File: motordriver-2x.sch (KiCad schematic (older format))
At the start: 330 parts

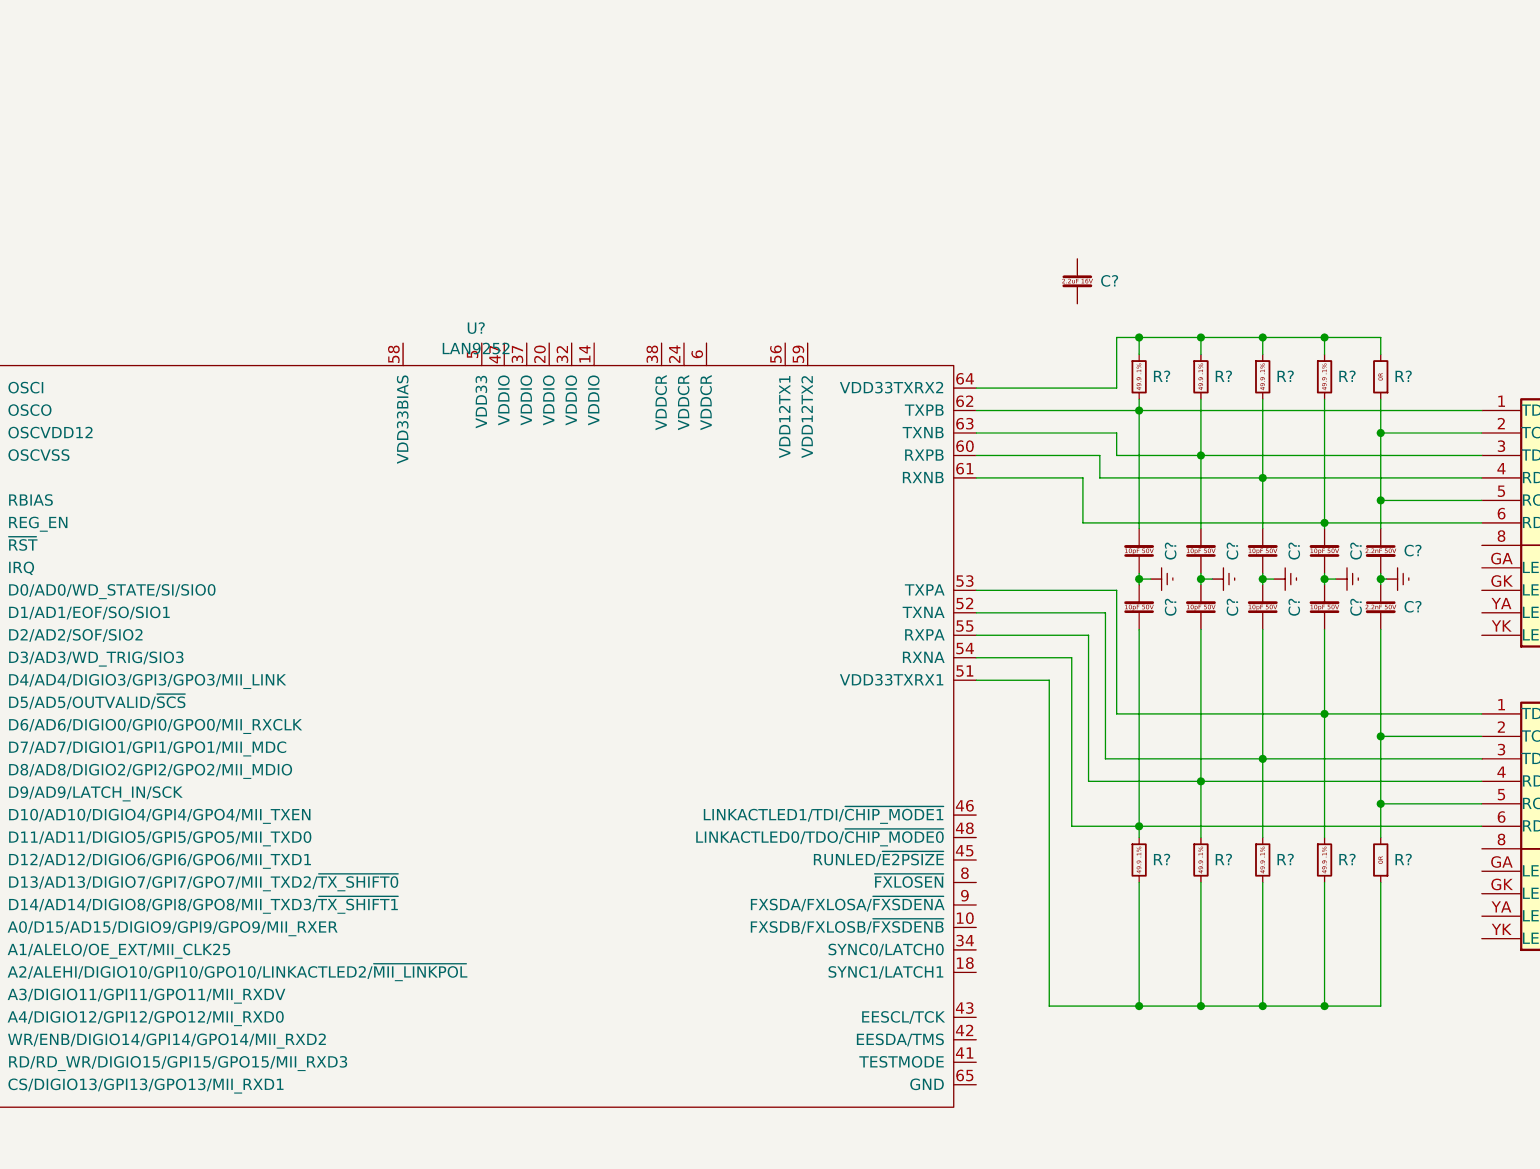
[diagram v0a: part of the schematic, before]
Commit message: add lcd connector
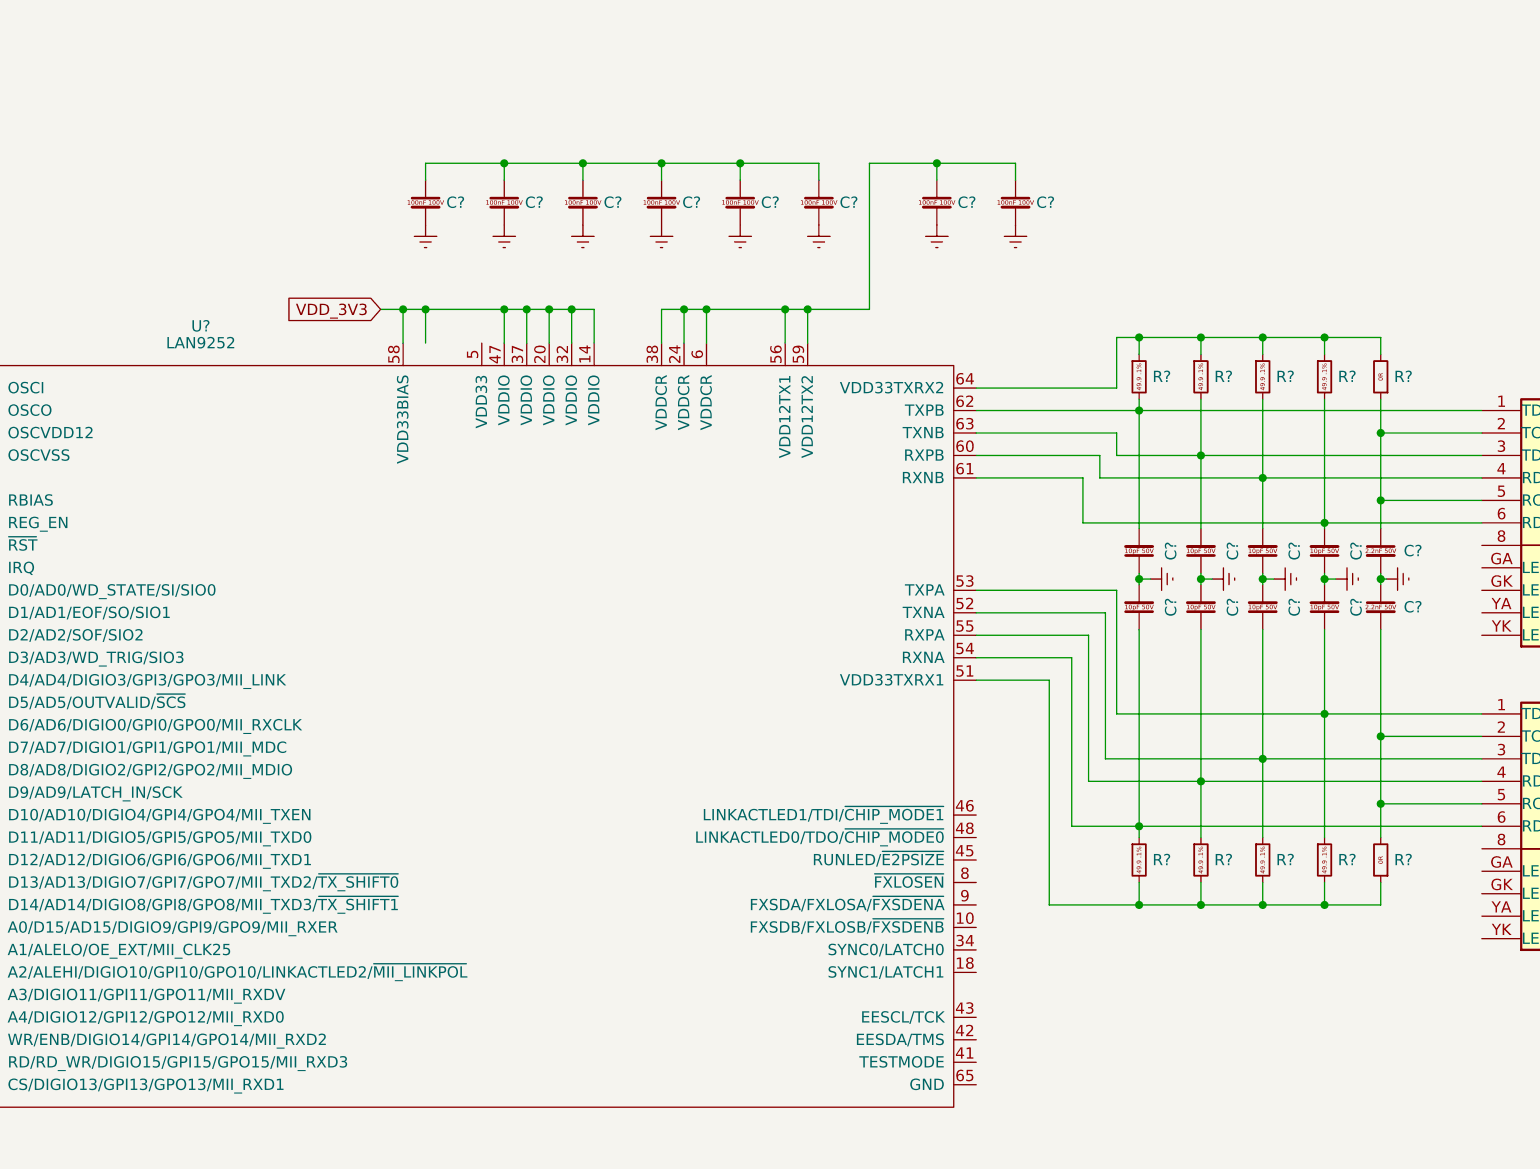
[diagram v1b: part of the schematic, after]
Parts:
- removed C?: CAP_2.2uF_16V_0402, Capacitor_SMD:C_0402_1005Metric, symbol SwEmb:CAP_2.2uF_16V_0402
- added C? (x8): CAP_100nF_100V_0603, Capacitor_SMD:C_0603_1608Metric, symbol SwEmb:CAP_100nF_100V_0603
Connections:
- wire segments 1049 -> 1089

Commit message: work on the ethercat circuit
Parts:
- added C? (x3): CAP_100nF_100V_0603, Capacitor_SMD:C_0603_1608Metric, symbol SwEmb:CAP_100nF_100V_0603
- added C? (x2): CAP_10pF_50V_0402, Capacitor_SMD:C_0402_1005Metric, symbol SwEmb:CAP_10pF_50V_0402
- added C?: CAP_100nF_50V_0402, Capacitor_SMD:C_0402_1005Metric, symbol SwEmb:CAP_100nF_50V_0402
- added D?: D_BAT54S, Package_TO_SOT_SMD:SOT-23, symbol SwEmb:D_BAT54S
- added FB? (x4): LB_220R_2A_0603, Inductor_SMD:L_0603_1608Metric, symbol SwEmb:LB_220R_2A_0603
- added R?: RES_12.1K_1%_0402, Resistor_SMD:R_0402_1005Metric, symbol SwEmb:RES_12.1K_1%_0402
- added R? (x7): RES_10K_1%_0402, Resistor_SMD:R_0402_1005Metric, symbol SwEmb:RES_10K_1%_0402
- added R? (x2): RES_3K_1%_0402, Resistor_SMD:R_0402_1005Metric, symbol SwEmb:RES_3K_1%_0402
- added R? (x2): RES_270R_1%_0402, Resistor_SMD:R_0402_1005Metric, symbol SwEmb:RES_270R_1%_0402
- added U?: IC_M24C02, Package_SO:SOIC-8_3.9x4.9mm_P1.27mm, symbol SwEmb:IC_M24C16
- added Y?: XTAL_25MHz_3225, Crystal:Crystal_SMD_3225-4Pin_3.2x2.5mm, symbol SwEmb:XTAL_25MHz_3225
- U?: symbol SwEmb:IC_M24C02 -> SwEmb:IC_M24C16
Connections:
- net labels added: ECAT_CS, ECAT_IRQ, ECAT_MISO, ECAT_MOSI, ECAT_RESET, ECAT_SCK, ECAT_SYNC0, ECAT_SYNC1
- wire segments 1089 -> 1191
- no-connect marks 30 -> 38
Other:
- note added: "150mA"

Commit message: add main power
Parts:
- added C?: CAPP_220uF_63V_10x15_THT, Capacitor_THT:CP_Radial_D10.0mm_P5.00mm, symbol SwEmb:CAPP_220uF_63V_10x15_THT
- added C?: CAP_27nF_16V_0402, Capacitor_SMD:C_0402_1005Metric, symbol SwEmb:CAP_27nF_16V_0402
- added C?: CAP_100nF_50V_0402, Capacitor_SMD:C_0402_1005Metric, symbol SwEmb:CAP_100nF_50V_0402
- added C?: CAP_51pF_50V_0402, Capacitor_SMD:C_0402_1005Metric, symbol SwEmb:CAP_51pF_50V_0402
- added C?: CAPP_100uF_25V_6357, Capacitor_SMD:CP_Elec_6.3x5.7, symbol SwEmb:CAPP_100uF_25V_6357
- added D?: D_CDBC5100, Diode_SMD:D_SMC, symbol SwEmb:D_CDBC5100
- added L?: L_100uH_3.64A, CUSTOM:L_Wuerth_WE-PD-Typ-LS_1250x1250, symbol SwEmb:L_100uH_3.64A
- added R?: RES_1M_1%_0402, Resistor_SMD:R_0402_1005Metric, symbol SwEmb:RES_1M_1%_0402
- added R?: RES_5K_1%_0402, Resistor_SMD:R_0402_1005Metric, symbol SwEmb:RES_5K_1%_0402
- added R?: RES_10K_1%_0402, Resistor_SMD:R_0402_1005Metric, symbol SwEmb:RES_10K_1%_0402
- added R?: RES_147k_1%_0603, Resistor_SMD:R_0603_1608Metric, symbol SwEmb:RES_147k_1%_0603
- added R?: RES_10.5k_1%_0603, Resistor_SMD:R_0603_1608Metric, symbol SwEmb:RES_10.5k_1%_0603
- added U?: IC_TPS54360DDA, SOIC:SOIC127P600X175_HS-9N, symbol SwEmb:IC_TPS54360DDA
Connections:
- net GNDREF: now also D?.1, D?.1, D?.1, D?.1, D?.1, D?.1, D?.1, C?.2, C?.2, C?.2, C?.2, D?.2 (A), R?.2, R?.2, U?.7 (GND), U?.9 (GNDPAD)
- net VDD_3V3: now also D?.2, D?.2, D?.2, D?.2, D?.2, D?.2, D?.2
- net VMOT_SENSE: now also D?.3
- net VSA1: now also D?.3
- net VSA2: now also D?.3
- net VSB1: now also D?.3
- net VSB2: now also D?.3
- net VSC1: now also D?.3
- net VSC2: now also D?.3
- new net: C?.2, U?.1 (BOOT)
- new net: C?.1, U?.2 (VIN)
- new net: R?.1, U?.4 (RT/CLK)
- new net: R?.1, R?.2, U?.5 (FB)
- new net: C?.1, R?.1, U?.6 (COMP)
- new net: C?.1, D?.1 (K), L?.1, U?.8 (SW)
- new net: C?.1, R?.2
- new net: R?.1, R?.2
- new net: C?.1, L?.2, R?.1
- no-connect marks 38 -> 39

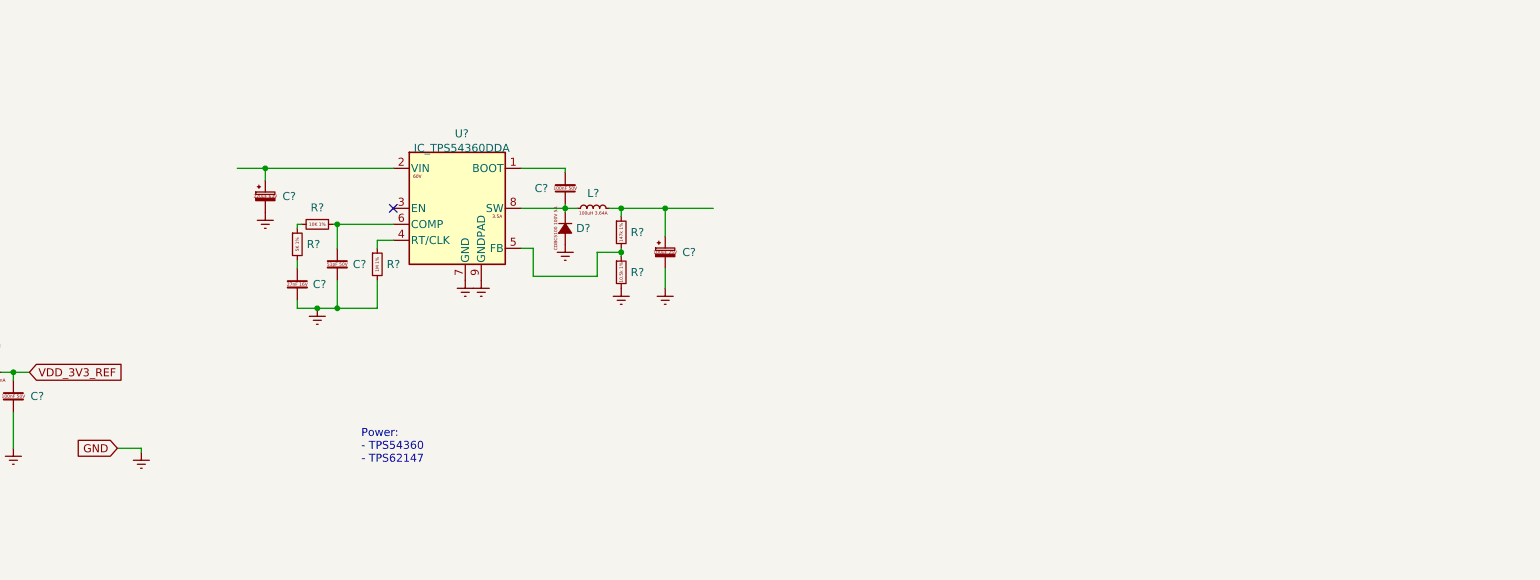
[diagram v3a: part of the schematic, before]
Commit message: add power supplies
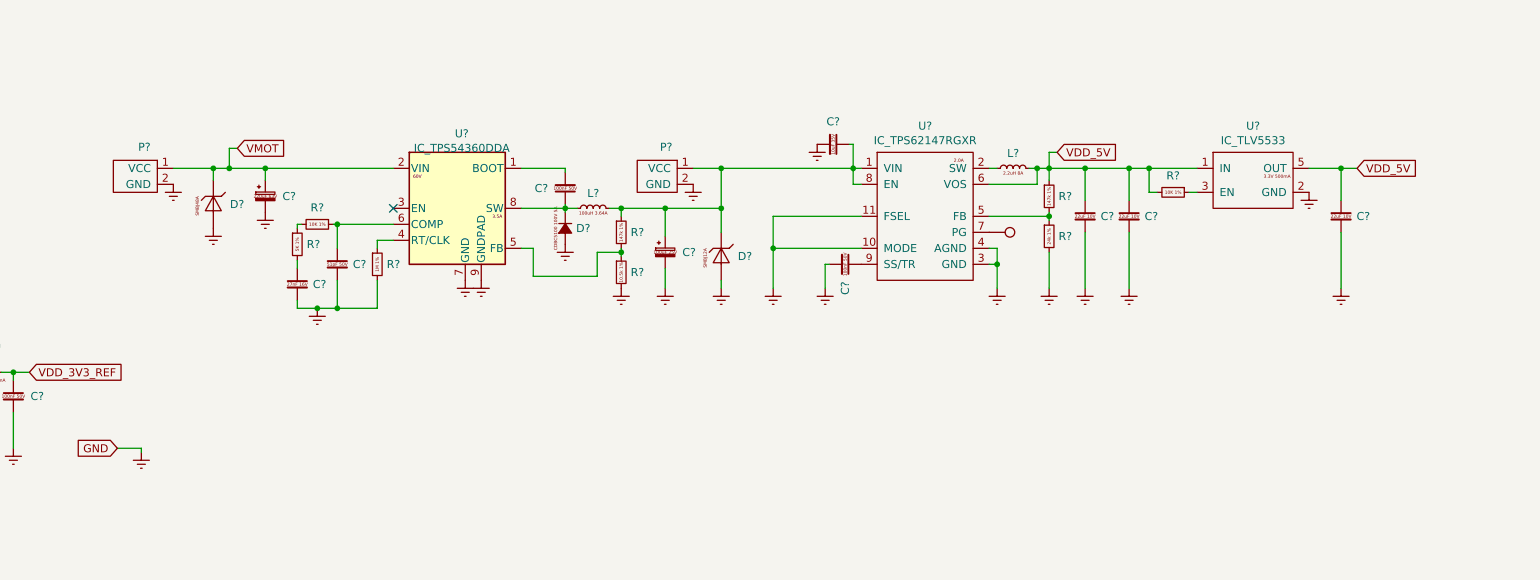
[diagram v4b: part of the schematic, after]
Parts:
- added C?: CAP_100nF_50V_0402, Capacitor_SMD:C_0402_1005Metric, symbol SwEmb:CAP_100nF_50V_0402
- added C? (x3): CAP_22uF_10V_0805, Capacitor_SMD:C_0805_2012Metric, symbol SwEmb:CAP_22uF_10V_0805
- added C?: CAP_10uF_35V_0603, Capacitor_SMD:C_0603_1608Metric, symbol SwEmb:CAP_10uF_35V_0603
- added D?: D_SMBJ48A, symbol SwEmb:D_SMBJ48A
- added D?: D_SMBJ12A, symbol SwEmb:D_SMBJ12A
- added L?: L_2.2uH_8A, Inductor_SMD:L_Coilcraft_XxL4020, symbol SwEmb:L_2.2uH_8A
- added P?: CONN_POWER_41A, CUSTOM:PhoenixContact_Power41A_2,5_2-G-7,62_1x02_P7.62mm_Horizontal, symbol SwEmb:CONN_POWER_41A
- added P?: CONN_POWER_10A, TerminalBlock_4Ucon:TerminalBlock_4Ucon_1x02_P3.50mm_Horizontal, symbol SwEmb:CONN_POWER_10A
- added R?: RES_147k_1%_0603, Resistor_SMD:R_0603_1608Metric, symbol SwEmb:RES_147k_1%_0603
- added R?: RES_24k_1%_0603, Resistor_SMD:R_0603_1608Metric, symbol SwEmb:RES_24k_1%_0603
- added R?: RES_10K_1%_0402, Resistor_SMD:R_0402_1005Metric, symbol SwEmb:RES_10K_1%_0402
- added TP?: Test_Point, TestPoint:TestPoint_Pad_1.0x1.0mm, symbol SwEmb:Test_Point
- added U?: IC_TPS62147RGXR, CUSTOM:RGX_VQFN-11, symbol SwEmb:IC_TPS62147RGXR
- added U?: IC_TLV5533, Package_TO_SOT_SMD:SOT-23-5, symbol SwEmb:IC_TLV5533
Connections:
- net GNDREF: now also C?.2, C?.2, C?.2, C?.2, C?.2, D?.2 (A), D?.2 (A), P?.2 (GND), P?.2 (GND), R?.2, U?.10 (MODE), U?.11 (FSEL), U?.2 (GND), U?.3 (GND), U?.4 (AGND)
- net VDD_5V: now also C?.1, C?.1, C?.1, L?.2, R?.1, R?.2, U?.1 (IN), U?.5 (OUT), U?.6 (VOS)
- net VMOT: now also C?.1, U?.2 (VIN), D?.1 (K), P?.1 (VCC)
- net at C?.1, L?.2, R?.1: now also C?.1, D?.1 (K), P?.1 (VCC), U?.1 (VIN), U?.8 (EN)
- new net: L?.1, U?.2 (SW)
- new net: R?.1, R?.2, U?.5 (FB)
- new net: TP?.1, U?.7 (PG)
- new net: C?.1, U?.9 (SS/TR)
- new net: R?.1, U?.3 (EN)
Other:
- note removed: "Power: \n- TPS54360\n- TPS62147"

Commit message: cleanup schematic
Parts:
- added D?: D_BAT54S, Package_TO_SOT_SMD:SOT-23, symbol SwEmb:D_BAT54S
- added D?: D_MM3Z3V3B, Diode_SMD:D_SOD-323F, symbol SwEmb:D_MM3Z3V3B
- added FB?: LB_220R_2A_0603, Inductor_SMD:L_0603_1608Metric, symbol SwEmb:LB_220R_2A_0603
- added TP? (x3): Test_Point, TestPoint:TestPoint_Pad_1.0x1.0mm, symbol SwEmb:Test_Point
- C? (x38): Availability 359167 In Stock -> 120297 In Stock; Description Multilayer Ceramic Capacitors MLCC - SMD/SMT 0402 0.1uF 50v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 -> Multilayer Ceramic Capacitors MLCC - SMD/SMT 100K pF 50Volt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; LifeCycle Not Recommended for New Designs -> OK; MPN GRM155R71H104ME14D -> CC0402KRX5R9BB104
- D?: footprint (none) -> Diode_SMD:D_SMB; Availability (none) -> 12398 In Stock; Description (none) -> ESD Suppressors / TVS Diodes 600W 48V Unidirect; LifeCycle (none) -> OK; Price (none) -> 0.314 EUR; Vendor (none) -> Mouser
- D?: footprint (none) -> Diode_SMD:D_SMB; Availability (none) -> 11297 In Stock; Description (none) -> ESD Suppressors / TVS Diodes 600W 12V Unidirect; LifeCycle (none) -> OK; Price (none) -> 0.314 EUR; Vendor (none) -> Mouser
- FB? (x4): Availability 65660 In Stock -> 193480 In Stock; Description Thick Film Resistors - SMD 1/10W 13K ohm 1% AEC-Q200 -> Ferrite Beads 220ohms GHz General Usage; Price 0.087 EUR -> 0.201 EUR; Vendor (none) -> Mouser
- L?: Availability 985 In Stock -> 8402 In Stock; Description Fixed Inductors 15uH 20% SMD 1260 AEC-Q200 -> Fixed Inductors 100uH 3.64A 0.163ohms; Price 0.934 EUR -> 1.77 EUR; Vendor (none) -> Mouser
- P?: footprint Connector_PinHeader_2.54mm:PinHeader_2x05_P2.54mm_Vertical -> Connector_PinSocket_2.54mm:PinSocket_2x05_P2.54mm_Vertical; MPN # -> N2510-6002RB
- P?: Availability (none) -> 357 In Stock; Description (none) -> Pluggable Terminal Blocks 2 Pos 7.62mm pitch Through Hole H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; LifeCycle (none) -> OK; Price (none) -> 2.68 EUR; Vendor (none) -> Mouser
- R?: Availability 1570651 In Stock -> 336681 In Stock; Description Thick Film Resistors - SMD 1.5K OHM 1% -> Thick Film Resistors - SMD 12.1K OHM 1%; Vendor (none) -> Mouser
- R?: Availability 93114 In Stock -> 179806 In Stock; Description Thick Film Resistors - SMD 147K OHM 1% -> Thick Film Resistors - SMD 24K ohm 1%; Vendor (none) -> Mouser
- U? (x2): value IC_M24C02 -> IC_M24C16; Availability 28402 In Stock -> 14758 In Stock; Description EEPROM EEPROM S I2C 2K -> EEPROM 16Kbit 8Kbit 4Kbit 2Kb and 1Kb Serial; MPN M24C02-WMN6TP -> M24C16-RMN6TP; Price 0.122 EUR -> 0.175 EUR
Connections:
- net GNDREF: now also D?.2 (A)
- net VDD_3V3: now also C?.1, U?.5 (OUT), D?.1 (K)
- net VDD_5V: now also D?.3, TP?.1; no longer C?.1, U?.5 (OUT)
- net VDD_5V_DBG_IN: now also D?.1
- net VMOT: now also TP?.1
- net VREF1: now reaches U?.32 (VREF+)
- net VREF1: now also C?.1, C?.1, U?.24 (REF), U?.24 (REF), U?.33 (VDDA), FB?.2
- net at C?.1, C?.1, D?.1 (K)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: now also TP?.1
- removed net VDD_3V3_REF: C?.1, C?.1, C?.1, U?.2 (OUT), U?.24 (REF), U?.24 (REF), U?.33 (VDDA)
- new net: C?.1, FB?.1, U?.2 (OUT)
- no-connect marks 39 -> 40
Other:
- note added: "Add possibility to bypass"
- note added: "Add possibility to bypass power"
- note added: "Motor Sensors 1"
- note added: "Motor Sensors 2"
- note added: "Power"
- note added: "Use extra inputs for HALL?\nAdd possibility to bypass"
- moved on the sheet: C?, D?, L?, P?, R?, U?
